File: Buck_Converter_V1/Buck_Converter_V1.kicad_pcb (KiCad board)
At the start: 2 copper layers, 75 x 40 mm, 28 parts, among them J1 Conn_01x01_Male, J2 Conn_01x01_Male, J3 Conn_01x01_Male, J4 Conn_01x01_Male, Q1 SI2319CDS-T1-GE3, U1 TL5001CDR

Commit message: Finished PCB layout. Ready for Gerber files.
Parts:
- moved C7 5.68 mm to (134.8, 83.0)
- moved C1 5.68 mm to (149.5, 81.9)
- moved R1 5.67 mm to (149.5, 80.0)
- moved C3 5.67 mm to (149.5, 83.7)
- moved RV2 5.67 mm to (138.0, 74.0)
- moved RV1 5.67 mm to (149.0, 74.0)
- moved U1 5.67 mm to (140.0, 81.1)
- moved C4 5.61 mm to (134.8, 79.1)
- moved C5 5.52 mm to (131.8, 82.1)
- moved R3 5.34 mm to (128.7, 83.0)
- moved R5 5.30 mm to (130.8, 79.1)
- moved R4 5.19 mm to (128.0, 80.0)
- moved C8 5.14 mm to (127.9, 78.1)
- moved D1 1.89 mm to (142.8, 96.3)
- moved L1 1.54 mm to (153.6, 92.9)
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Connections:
- IN- pad 1: (no net) -> GND
- OUT+ pad 1: (no net) -> Vout
- OUT- pad 1: (no net) -> GND
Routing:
- net Vout: track 0.00 -> 44.0 mm, vias 0 -> 2
- net Net-(C7-Pad1): track 0.00 -> 27.4 mm
- net Vin: track 0.00 -> 21.6 mm, vias 0 -> 2
- net P_DRIVE: track 0.00 -> 14.0 mm
- net Net-(RV1-Pad2): track 0.00 -> 12.1 mm
- net Net-(C1-Pad1): track 0.00 -> 7.83 mm
- net Net-(C3-Pad2): track 0.00 -> 6.23 mm
- net Net-(C5-Pad2): track 0.00 -> 4.81 mm
- net Net-(C5-Pad1): track 0.00 -> 2.18 mm
- net Net-(C8-Pad2): track 0.00 -> 2.06 mm
- net GND: vias 0 -> 21
- net (no net): vias 1 -> 0
- added copper zone on B.Cu, net GND
- added copper zone on F.Cu, net GND
- added copper zone on F.Cu, net Net-(D1-Pad1)
- added copper zone on F.Cu, net Net-(F1-Pad2)
- added copper zone on F.Cu, net Vin
- added copper zone on F.Cu, net Vout
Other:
- board text added: "Buck Converter V1"
- board text added: "Min Vin = 3.6V Max Vin = 20V Max Iout = 3A"

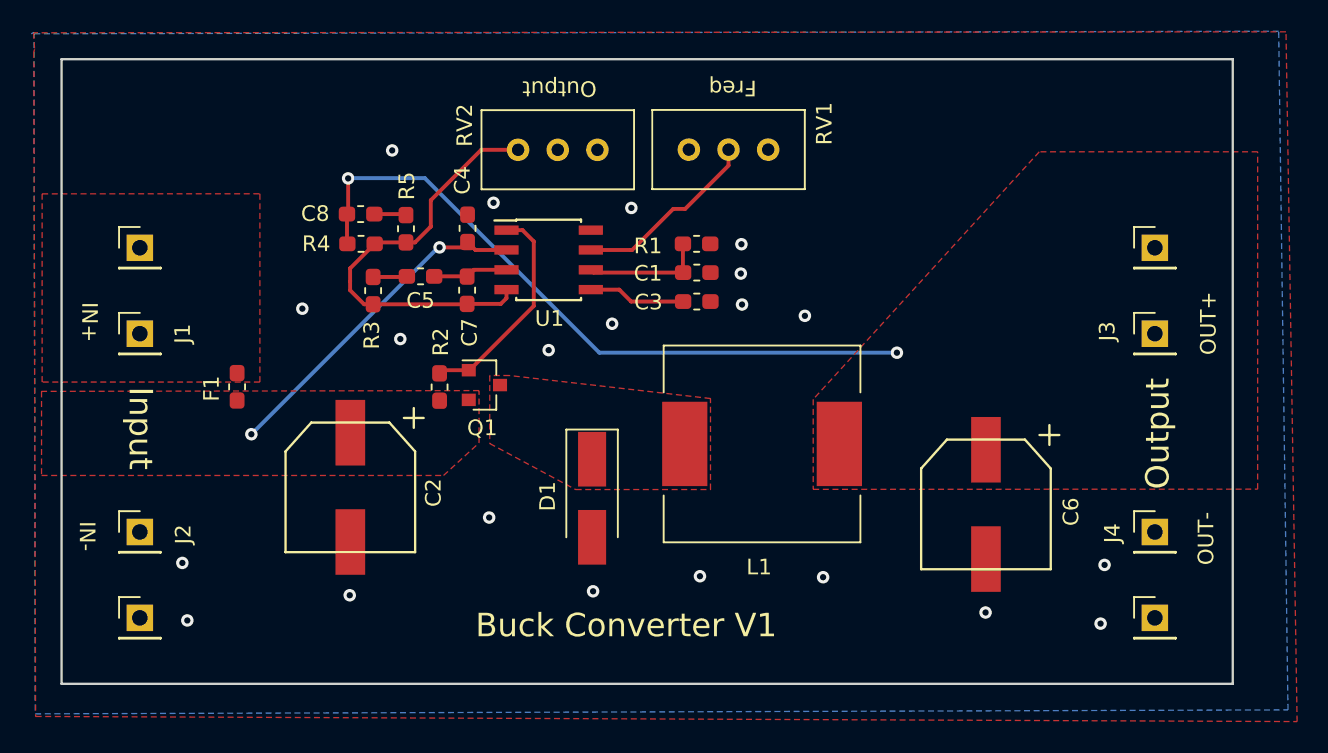
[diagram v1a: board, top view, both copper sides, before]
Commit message: Changed out+ and out- pads to be 7.62mm apart to make it easy to attach USB breakout board.
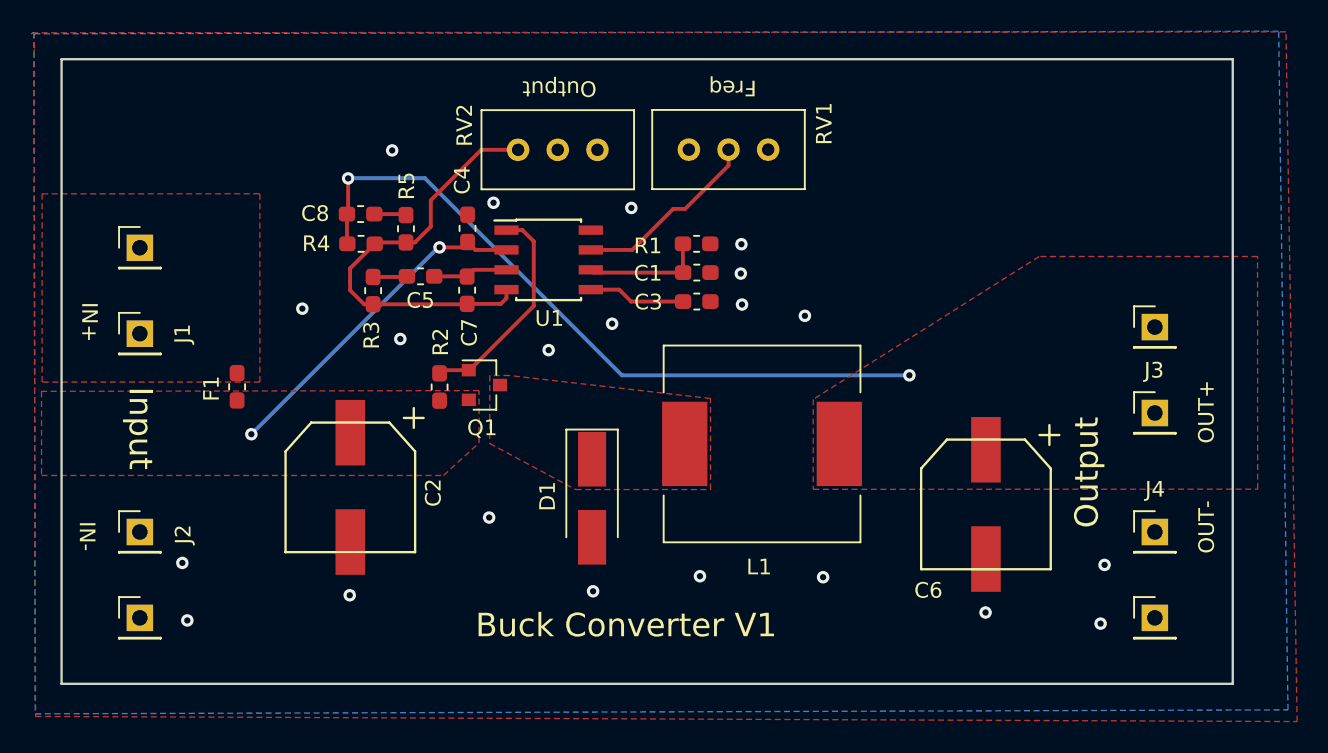
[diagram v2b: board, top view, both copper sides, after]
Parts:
- moved J3 5.08 mm to (178.8, 90.9)
- moved OUT+ 5.08 mm to (178.8, 85.4)
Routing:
- net Vout: track 44.0 -> 45.4 mm
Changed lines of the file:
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@@
   )
   (module Connector_PinHeader_2.54mm:PinHeader_1x01_P2.54mm_Vertical (layer F.Cu)
-    (at 178.8 80.3)
+    (at 178.8 85.38)
     (descr "Through hole straight pin header, 1x01, 2.54mm pitch, single row")
     (tags "Through hole pin header THT 1x01 2.54mm single row")
-    (fp_text reference OUT+ (at 3.429 4.8387 90 unlocked) (layer F.SilkS)
+    (fp_text reference OUT+ (at 3.3053 5.425 90 unlocked) (layer F.SilkS)
       (effects (font (size 1 1) (thickness 0.15)))
     )
@@
     (descr "Through hole straight pin header, 1x01, 2.54mm pitch, single row")
     (tags "Through hole pin header THT 1x01 2.54mm single row")
-    (fp_text reference OUT- (at 3.2766 -5.08 90 unlocked) (layer F.SilkS)
+    (fp_text reference OUT- (at 3.318 -5.8163 90 unlocked) (layer F.SilkS)
       (effects (font (size 1 1) (thickness 0.15)))
     )
@@
   (module Custom_Footprints:C_AlPo_Radial_SMT_8.3mmx8.3mm (layer F.Cu)
     (at 167.9829 96.7359 270)
-    (fp_text reference C6 (at 0.4699 -5.4483 270) (layer F.SilkS)
+    (fp_text reference C6 (at 5.5118 3.683) (layer F.SilkS)
       (effects (font (size 1 1) (thickness 0.15)))
     )
@@
   )
   (module Connector_PinHeader_2.54mm:PinHeader_1x01_P2.54mm_Vertical (layer F.Cu)
-    (at 178.8 85.8)
+    (at 178.8 90.88)
     (descr "Through hole straight pin header, 1x01, 2.54mm pitch, single row")
     (tags "Through hole pin header THT 1x01 2.54mm single row")
-    (fp_text reference J3 (at -3.048 -0.1524 90) (layer F.SilkS)
+    (fp_text reference J3 (at -0.0475 -2.7293 180) (layer F.SilkS)
       (effects (font (size 1 1) (thickness 0.15)))
     )
@@
     (descr "Through hole straight pin header, 1x01, 2.54mm pitch, single row")
     (tags "Through hole pin header THT 1x01 2.54mm single row")
-    (fp_text reference J4 (at -2.7178 0.0762 90) (layer F.SilkS)
+    (fp_text reference J4 (at 0.016 -2.7293 180) (layer F.SilkS)
       (effects (font (size 1 1) (thickness 0.15)))
     )
@@
   (gr_line (start 183.7882 68.2244) (end 183.7882 108.2244) (layer Edge.Cuts) (width 0.15))
   (gr_line (start 108.7882 68.2244) (end 183.7882 68.2244) (layer Edge.Cuts) (width 0.15))
-  (gr_text Output (at 178.9811 92.202 90) (layer F.SilkS)
+  (gr_text Output (at 174.4472 94.6912 90) (layer F.SilkS)
     (effects (font (size 1.5 1.5) (thickness 0.3)))
   )
@@
     (effects (font (size 1 1) (thickness 0.25)))
   )
-  (via (at 132.9944 80.2767) (size 0.8) (drill 0.4) (layers F.Cu B.Cu) (net 3))
-  (via (at 152.3238 80.0735) (size 0.8) (drill 0.4) (layers F.Cu B.Cu) (net 2))
   (segment (start 142.8572 81.8896) (end 142.6794 81.7118) (width 0.25) (layer F.Cu) (net 1))
   (segment (start 148.5913 81.8896) (end 142.8572 81.8896) (width 0.25) (layer F.Cu) (net 1))
   (segment (start 148.5786 81.8769) (end 148.5913 81.8896) (width 0.25) (layer F.Cu) (net 1))
   (segment (start 148.5786 80.0481) (end 148.5786 81.8769) (width 0.25) (layer F.Cu) (net 1))
+  (via (at 152.3238 80.0735) (size 0.8) (drill 0.4) (layers F.Cu B.Cu) (net 2))
   (via (at 152.2857 81.9531) (size 0.8) (drill 0.4) (layers F.Cu B.Cu) (net 2))
   (via (at 152.3619 83.9343) (size 0.8) (drill 0.4) (layers F.Cu B.Cu) (net 2))
@@
   (via (at 149.6695 101.3333) (size 0.8) (drill 0.4) (layers F.Cu B.Cu) (net 2))
   (via (at 156.3878 84.6582) (size 0.8) (drill 0.4) (layers F.Cu B.Cu) (net 2))
+  (via (at 132.9944 80.2767) (size 0.8) (drill 0.4) (layers F.Cu B.Cu) (net 3))
   (via (at 120.9421 92.2401) (size 0.8) (drill 0.4) (layers F.Cu B.Cu) (net 3))
   (segment (start 135.2944 80.4418) (end 134.7851 79.9325) (width 0.25) (layer F.Cu) (net 3))
@@
   (segment (start 135.1928 81.7118) (end 134.7597 82.1449) (width 0.25) (layer F.Cu) (net 6))
   (segment (start 137.2794 81.7118) (end 135.1928 81.7118) (width 0.25) (layer F.Cu) (net 6))
-  (via (at 162.2806 87.0204) (size 0.8) (drill 0.4) (layers F.Cu B.Cu) (net 7))
-  (segment (start 162.2806 87.0204) (end 143.2306 87.0204) (width 0.25) (layer B.Cu) (net 7))
-  (segment (start 143.2306 87.0204) (end 132.0546 75.8444) (width 0.25) (layer B.Cu) (net 7))
-  (segment (start 132.0546 75.8444) (end 127.1524 75.8444) (width 0.25) (layer B.Cu) (net 7))
+  (via (at 163.0807 88.4682) (size 0.8) (drill 0.4) (layers F.Cu B.Cu) (net 7))
   (via (at 127.1397 75.8571) (size 0.8) (drill 0.4) (layers F.Cu B.Cu) (net 7))
-  (segment (start 127.1524 75.8444) (end 127.1397 75.8571) (width 0.25) (layer B.Cu) (net 7))
   (segment (start 127.1397 78.0682) (end 127.0648 78.1431) (width 0.25) (layer F.Cu) (net 7))
   (segment (start 127.1397 75.8571) (end 127.1397 78.0682) (width 0.25) (layer F.Cu) (net 7))
   (segment (start 127.0648 80.0227) (end 127.0902 80.0481) (width 0.25) (layer F.Cu) (net 7))
   (segment (start 127.0648 78.1431) (end 127.0648 80.0227) (width 0.25) (layer F.Cu) (net 7))
+  (segment (start 127.1524 75.8444) (end 127.1397 75.8571) (width 0.25) (layer B.Cu) (net 7))
+  (segment (start 132.0546 75.8444) (end 127.1524 75.8444) (width 0.25) (layer B.Cu) (net 7))
+  (segment (start 163.0807 88.4682) (end 144.6784 88.4682) (width 0.25) (layer B.Cu) (net 7))
+  (segment (start 144.6784 88.4682) (end 132.0546 75.8444) (width 0.25) (layer B.Cu) (net 7))
   (segment (start 128.9304 79.9579) (end 128.8402 80.0481) (width 0.25) (layer F.Cu) (net 8))
   (segment (start 130.843134 79.9579) (end 128.9304 79.9579) (width 0.25) (layer F.Cu) (net 8))
@@
     (polygon
       (pts
-        (xy 156.9212 95.7707) (xy 185.3819 95.758) (xy 185.3819 74.1553) (xy 171.3992 74.1553) (xy 156.9212 90.0049)
+        (xy 156.9212 95.7707) (xy 185.3819 95.758) (xy 185.37555 80.8609) (xy 171.39285 80.8609) (xy 156.9212 90.0049)
         (xy 156.9212 95.758)
       )
@@
       )
     )
+  )
+  (zone (net 0) (net_name "") (layer B.Cu) (hatch edge 0.508)
+    (connect_pads (clearance 0.508))
+    (min_thickness 0.254)
+    (keepout (tracks not_allowed) (vias not_allowed) (copperpour not_allowed))
+    (fill (arc_segments 16) (thermal_gap 0.508) (thermal_bridge_width 0.508))
+    (polygon
+      (pts
+        (xy 111.2266 78.32109) (xy 111.252 87.74449) (xy 116.2939 87.74449) (xy 116.2939 78.33379) (xy 111.4298 78.32109)
+      )
+    )
+  )
+  (zone (net 0) (net_name "") (layer B.Cu) (hatch edge 0.508)
+    (connect_pads (clearance 0.508))
+    (min_thickness 0.254)
+    (keepout (tracks not_allowed) (vias not_allowed) (copperpour not_allowed))
+    (fill (arc_segments 16) (thermal_gap 0.508) (thermal_bridge_width 0.508))
+    (polygon
+      (pts
+        (xy 176.2633 83.397312) (xy 176.2887 92.820712) (xy 181.3306 92.820712) (xy 181.3306 83.410012) (xy 176.4665 83.397312)
+      )
+    )
